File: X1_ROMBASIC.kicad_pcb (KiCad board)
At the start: 2 copper layers, 137 x 140 mm, 0 parts

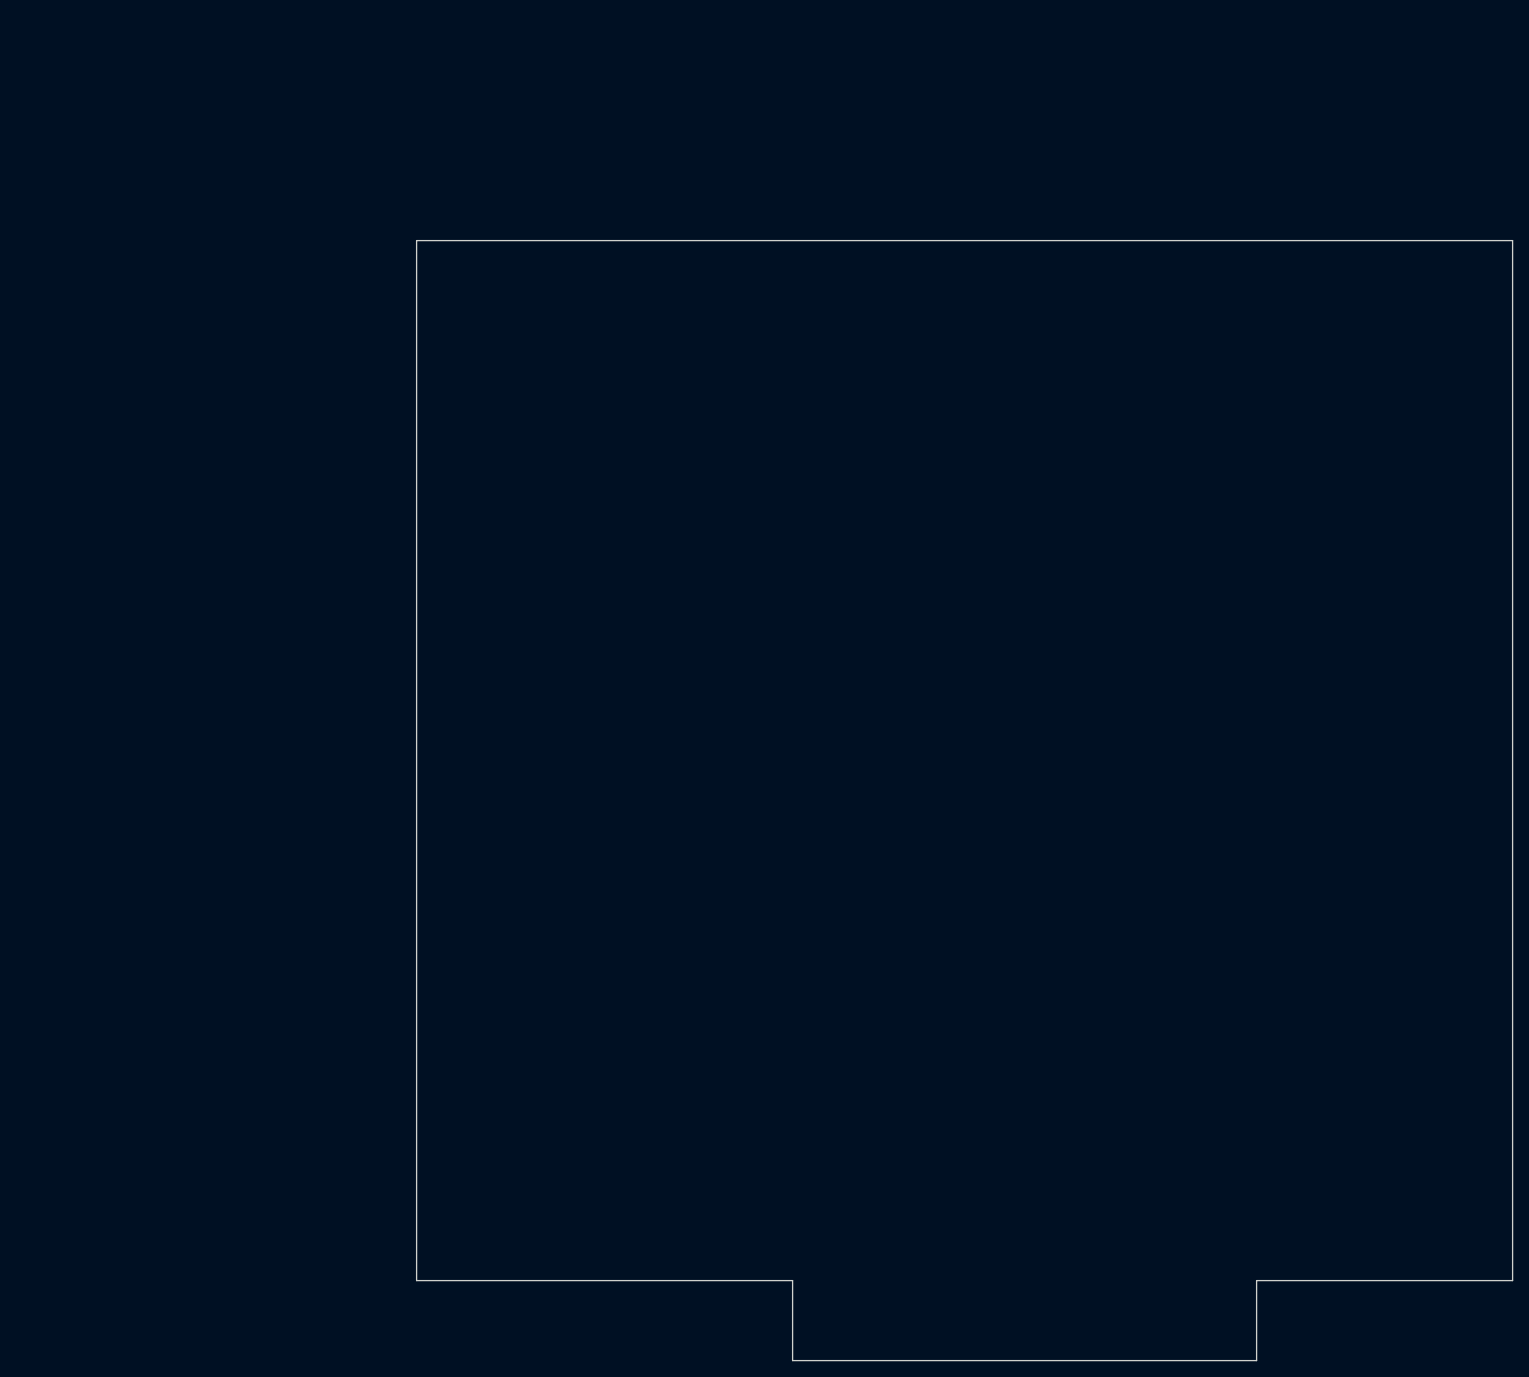
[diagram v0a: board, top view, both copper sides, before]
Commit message: フットプリントの追加
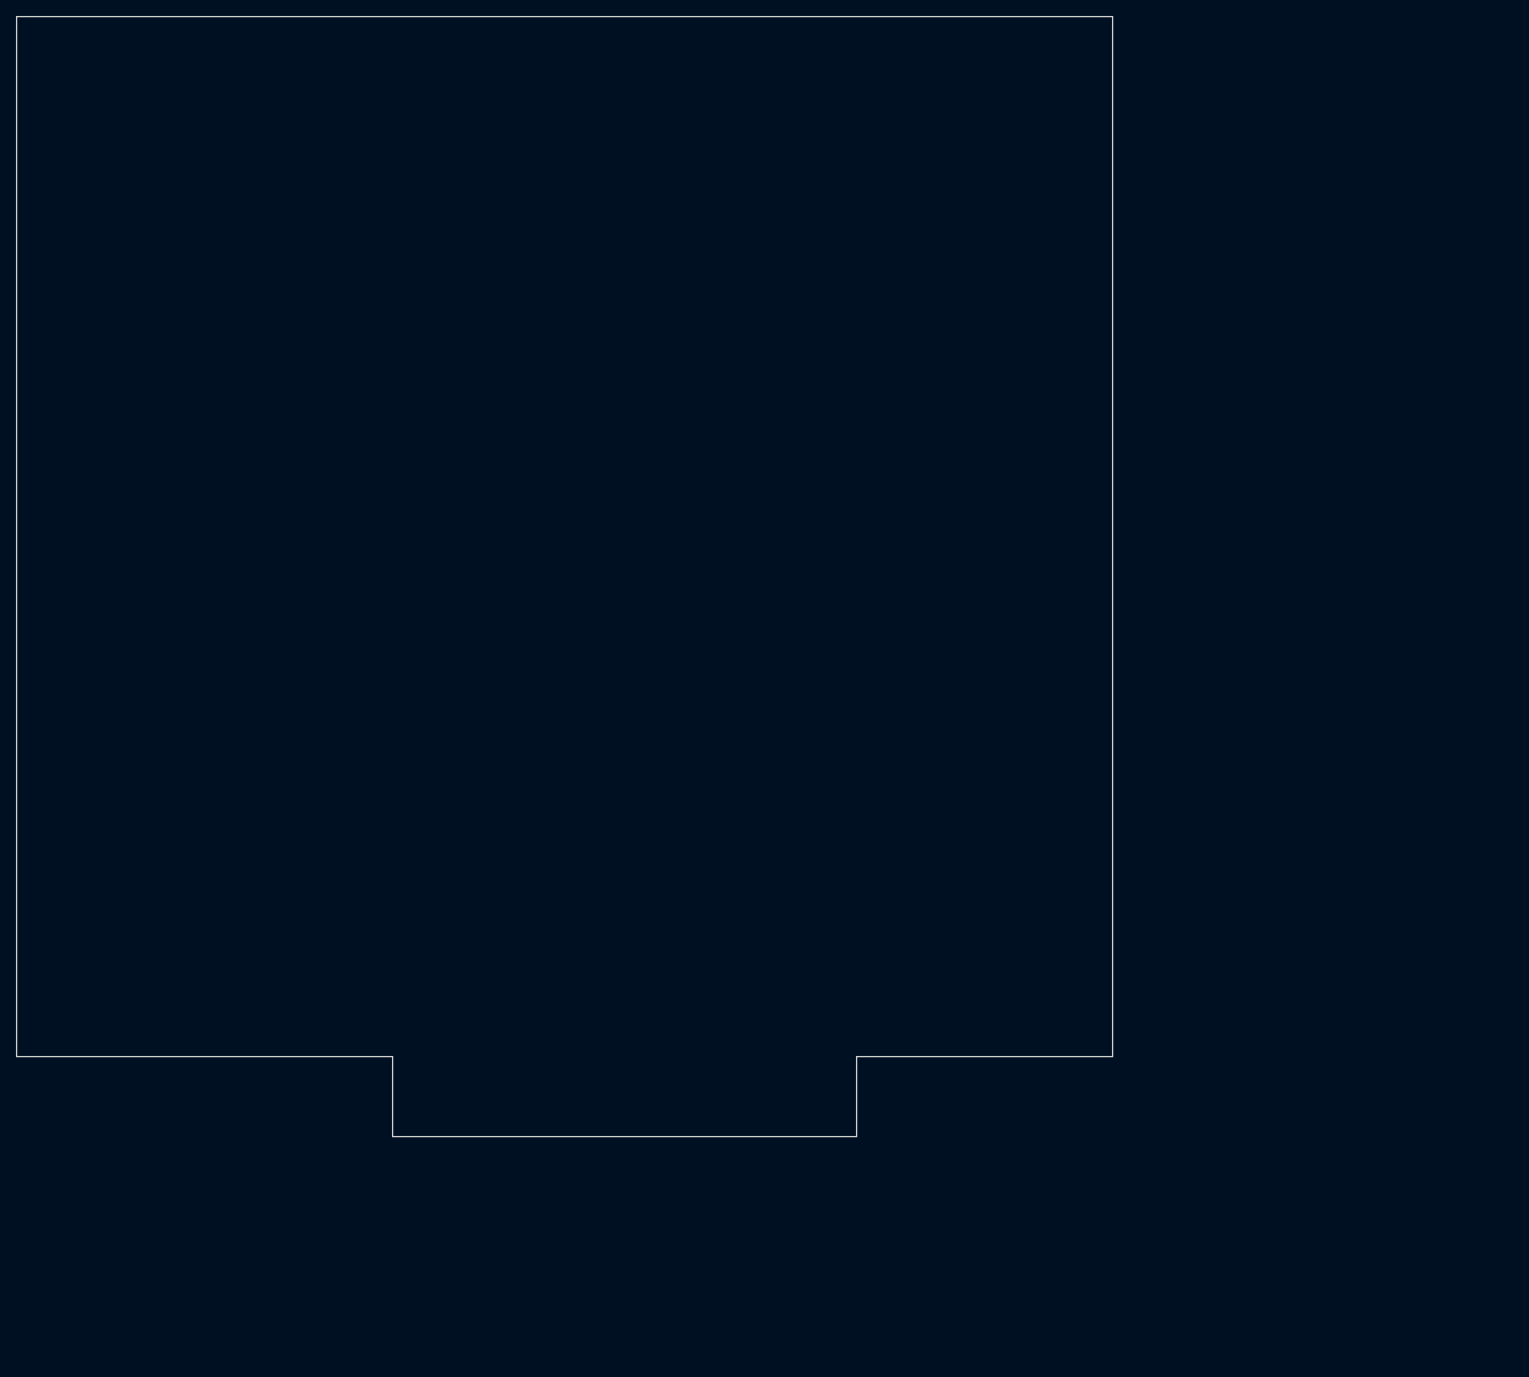
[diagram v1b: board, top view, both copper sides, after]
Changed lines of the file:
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@@
     (links 0)
     (no_connects 0)
-    (area 83.857144 60.150003 237.075001 221.7)
+    (area 33.857144 32.150003 187.075001 193.7)
     (thickness 1.6)
     (drawings 13)
@@
     (mod_text_size 1.5 1.5)
     (mod_text_width 0.15)
-    (pad_size 1.524 1.524)
-    (pad_drill 0.762)
+    (pad_size 1.5 10)
+    (pad_drill 0)
     (pad_to_mask_clearance 0.2)
     (aux_axis_origin 0 0)
@@
   )
   (dimension 32 (width 0.3) (layer Cmts.User)
-    (gr_text 32.000mm (at 221 220.349999) (layer Cmts.User)
+    (gr_text 32.000mm (at 171 192.349999) (layer Cmts.User)
       (effects (font (size 1.5 1.5) (thickness 0.3)))
     )
-    (feature1 (pts (xy 237 201) (xy 237 221.699999)))
-    (feature2 (pts (xy 205 201) (xy 205 221.699999)))
-    (crossbar (pts (xy 205 218.999999) (xy 237 218.999999)))
-    (arrow1a (pts (xy 237 218.999999) (xy 235.873497 219.586419)))
-    (arrow1b (pts (xy 237 218.999999) (xy 235.873497 218.413579)))
-    (arrow2a (pts (xy 205 218.999999) (xy 206.126503 219.586419)))
-    (arrow2b (pts (xy 205 218.999999) (xy 206.126503 218.413579)))
+    (feature1 (pts (xy 187 173) (xy 187 193.699999)))
+    (feature2 (pts (xy 155 173) (xy 155 193.699999)))
+    (crossbar (pts (xy 155 190.999999) (xy 187 190.999999)))
+    (arrow1a (pts (xy 187 190.999999) (xy 185.873497 191.586419)))
+    (arrow1b (pts (xy 187 190.999999) (xy 185.873497 190.413579)))
+    (arrow2a (pts (xy 155 190.999999) (xy 156.126503 191.586419)))
+    (arrow2b (pts (xy 155 190.999999) (xy 156.126503 190.413579)))
   )
   (dimension 47 (width 0.3) (layer Cmts.User)
-    (gr_text 47.000mm (at 123.5 220.349999) (layer Cmts.User)
+    (gr_text 47.000mm (at 73.5 192.349999) (layer Cmts.User)
       (effects (font (size 1.5 1.5) (thickness 0.3)))
     )
-    (feature1 (pts (xy 147 201) (xy 147 221.699999)))
-    (feature2 (pts (xy 100 201) (xy 100 221.699999)))
-    (crossbar (pts (xy 100 218.999999) (xy 147 218.999999)))
-    (arrow1a (pts (xy 147 218.999999) (xy 145.873497 219.586419)))
-    (arrow1b (pts (xy 147 218.999999) (xy 145.873497 218.413579)))
-    (arrow2a (pts (xy 100 218.999999) (xy 101.126503 219.586419)))
-    (arrow2b (pts (xy 100 218.999999) (xy 101.126503 218.413579)))
+    (feature1 (pts (xy 97 173) (xy 97 193.699999)))
+    (feature2 (pts (xy 50 173) (xy 50 193.699999)))
+    (crossbar (pts (xy 50 190.999999) (xy 97 190.999999)))
+    (arrow1a (pts (xy 97 190.999999) (xy 95.873497 191.586419)))
+    (arrow1b (pts (xy 97 190.999999) (xy 95.873497 190.413579)))
+    (arrow2a (pts (xy 50 190.999999) (xy 51.126503 191.586419)))
+    (arrow2b (pts (xy 50 190.999999) (xy 51.126503 190.413579)))
   )
   (dimension 10 (width 0.3) (layer Cmts.User)
-    (gr_text 10.000mm (at 137 207 270) (layer Cmts.User)
+    (gr_text 10.000mm (at 87 179 270) (layer Cmts.User)
       (effects (font (size 1.5 1.5) (thickness 0.3)))
     )
-    (feature1 (pts (xy 147 211) (xy 137.300001 211)))
-    (feature2 (pts (xy 147 201) (xy 137.300001 201)))
-    (crossbar (pts (xy 140.000001 201) (xy 140.000001 211)))
-    (arrow1a (pts (xy 140.000001 211) (xy 139.413581 209.873497)))
-    (arrow1b (pts (xy 140.000001 211) (xy 140.586421 209.873497)))
-    (arrow2a (pts (xy 140.000001 201) (xy 139.413581 202.126503)))
-    (arrow2b (pts (xy 140.000001 201) (xy 140.586421 202.126503)))
+    (feature1 (pts (xy 97 183) (xy 87.300001 183)))
+    (feature2 (pts (xy 97 173) (xy 87.300001 173)))
+    (crossbar (pts (xy 90.000001 173) (xy 90.000001 183)))
+    (arrow1a (pts (xy 90.000001 183) (xy 89.413581 181.873497)))
+    (arrow1b (pts (xy 90.000001 183) (xy 90.586421 181.873497)))
+    (arrow2a (pts (xy 90.000001 173) (xy 89.413581 174.126503)))
+    (arrow2b (pts (xy 90.000001 173) (xy 90.586421 174.126503)))
   )
-  (gr_line (start 147 211) (end 205 211) (angle 90) (layer Edge.Cuts) (width 0.15))
-  (gr_line (start 147 201) (end 147 211) (angle 90) (layer Edge.Cuts) (width 0.15))
-  (gr_line (start 100 201) (end 147 201) (angle 90) (layer Edge.Cuts) (width 0.15))
-  (gr_line (start 205 201) (end 205 211) (angle 90) (layer Edge.Cuts) (width 0.15))
-  (gr_line (start 237 201) (end 205 201) (angle 90) (layer Edge.Cuts) (width 0.15))
-  (gr_line (start 237 71) (end 237 201) (angle 90) (layer Edge.Cuts) (width 0.15))
+  (gr_line (start 97 183) (end 155 183) (angle 90) (layer Edge.Cuts) (width 0.15))
+  (gr_line (start 97 173) (end 97 183) (angle 90) (layer Edge.Cuts) (width 0.15))
+  (gr_line (start 50 173) (end 97 173) (angle 90) (layer Edge.Cuts) (width 0.15))
+  (gr_line (start 155 173) (end 155 183) (angle 90) (layer Edge.Cuts) (width 0.15))
+  (gr_line (start 187 173) (end 155 173) (angle 90) (layer Edge.Cuts) (width 0.15))
+  (gr_line (start 187 43) (end 187 173) (angle 90) (layer Edge.Cuts) (width 0.15))
   (dimension 130 (width 0.3) (layer Cmts.User)
-    (gr_text 130.000mm (at 90.65 136 270) (layer Cmts.User)
+    (gr_text 130.000mm (at 40.65 108 270) (layer Cmts.User)
       (effects (font (size 1.5 1.5) (thickness 0.3)))
     )
-    (feature1 (pts (xy 100 201) (xy 89.3 201)))
-    (feature2 (pts (xy 100 71) (xy 89.3 71)))
-    (crossbar (pts (xy 92 71) (xy 92 201)))
-    (arrow1a (pts (xy 92 201) (xy 91.41358 199.873497)))
-    (arrow1b (pts (xy 92 201) (xy 92.58642 199.873497)))
-    (arrow2a (pts (xy 92 71) (xy 91.41358 72.126503)))
-    (arrow2b (pts (xy 92 71) (xy 92.58642 72.126503)))
+    (feature1 (pts (xy 50 173) (xy 39.3 173)))
+    (feature2 (pts (xy 50 43) (xy 39.3 43)))
+    (crossbar (pts (xy 42 43) (xy 42 173)))
+    (arrow1a (pts (xy 42 173) (xy 41.41358 171.873497)))
+    (arrow1b (pts (xy 42 173) (xy 42.58642 171.873497)))
+    (arrow2a (pts (xy 42 43) (xy 41.41358 44.126503)))
+    (arrow2b (pts (xy 42 43) (xy 42.58642 44.126503)))
   )
   (dimension 137 (width 0.3) (layer Cmts.User)
-    (gr_text 137.000mm (at 168.5 61.650003) (layer Cmts.User)
+    (gr_text 137.000mm (at 118.5 33.650003) (layer Cmts.User)
       (effects (font (size 1.5 1.5) (thickness 0.3)))
     )
-    (feature1 (pts (xy 237 71) (xy 237 60.300003)))
-    (feature2 (pts (xy 100 71) (xy 100 60.300003)))
-    (crossbar (pts (xy 100 63.000003) (xy 237 63.000003)))
-    (arrow1a (pts (xy 237 63.000003) (xy 235.873497 63.586423)))
-    (arrow1b (pts (xy 237 63.000003) (xy 235.873497 62.413583)))
-    (arrow2a (pts (xy 100 63.000003) (xy 101.126503 63.586423)))
-    (arrow2b (pts (xy 100 63.000003) (xy 101.126503 62.413583)))
+    (feature1 (pts (xy 187 43) (xy 187 32.300003)))
+    (feature2 (pts (xy 50 43) (xy 50 32.300003)))
+    (crossbar (pts (xy 50 35.000003) (xy 187 35.000003)))
+    (arrow1a (pts (xy 187 35.000003) (xy 185.873497 35.586423)))
+    (arrow1b (pts (xy 187 35.000003) (xy 185.873497 34.413583)))
+    (arrow2a (pts (xy 50 35.000003) (xy 51.126503 35.586423)))
+    (arrow2b (pts (xy 50 35.000003) (xy 51.126503 34.413583)))
   )
-  (gr_line (start 100 71) (end 100 201) (angle 90) (layer Edge.Cuts) (width 0.15))
-  (gr_line (start 100 71) (end 237 71) (angle 90) (layer Edge.Cuts) (width 0.15))
+  (gr_line (start 50 43) (end 50 173) (angle 90) (layer Edge.Cuts) (width 0.15))
+  (gr_line (start 50 43) (end 187 43) (angle 90) (layer Edge.Cuts) (width 0.15))
 )
